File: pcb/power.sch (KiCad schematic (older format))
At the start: 6 parts

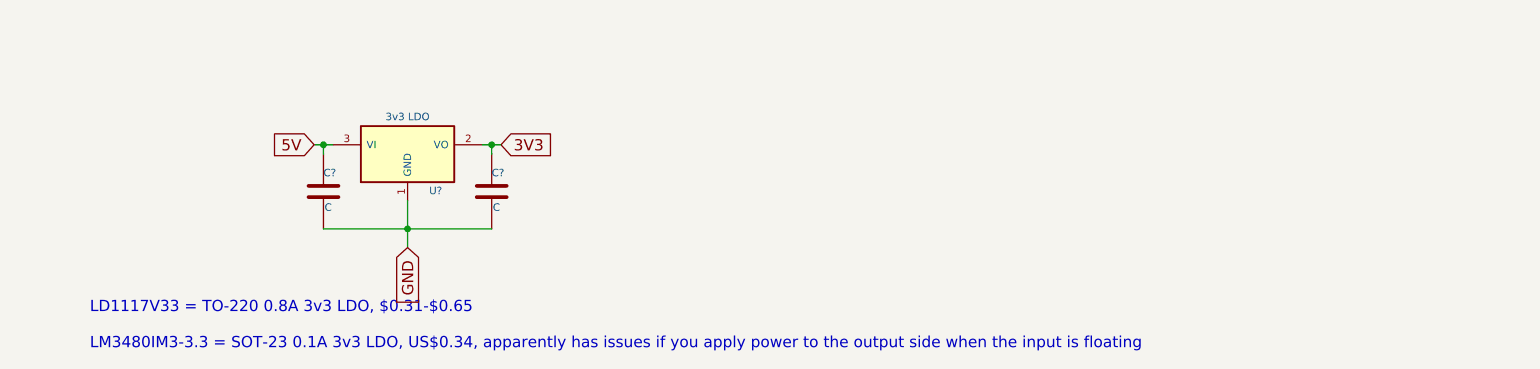
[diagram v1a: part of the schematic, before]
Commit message: added reset pullup, some caps, usb resistors, explanation for nUSB_CONNECT
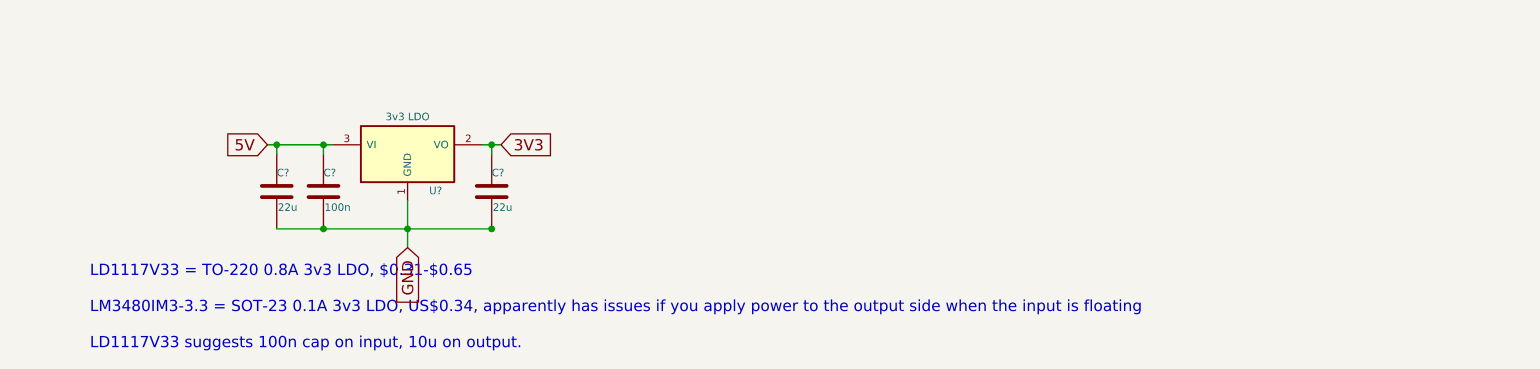
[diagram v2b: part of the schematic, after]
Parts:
- added C?: 22u, ~, symbol C
- C?: value C -> 100n
- C?: value C -> 22u
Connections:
- net 5V: now also C?.1
- net GND: now also C?.2
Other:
- note added: "LD1117V33 = TO-220 0.8A 3v3 LDO, $0.31-$0.65\n\nLM3480IM3-3.3 = SOT-23 0.1A 3v3 LDO, US$0.34, apparently has issues if you apply power to the output side when the input is floating\n\nLD1117V33 suggests 100n cap on input, 10u on output."
- note removed: "LD1117V33 = TO-220 0.8A 3v3 LDO, $0.31-$0.65\n\nLM3480IM3-3.3 = SOT-23 0.1A 3v3 LDO, US$0.34, apparently has issues if you apply power to the output side when the input is floating"
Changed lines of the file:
@@
 P 3300 4750
 F 0 "C?" H 3300 4850 40  0000 L CNN
-F 1 "C" H 3306 4665 40  0000 L CNN
+F 1 "100n" H 3306 4665 40  0000 L CNN
 F 2 "~" H 3338 4600 30  0000 C CNN
 F 3 "~" H 3300 4750 60  0000 C CNN
@@
 P 4200 4750
 F 0 "C?" H 4200 4850 40  0000 L CNN
-F 1 "C" H 4206 4665 40  0000 L CNN
+F 1 "22u" H 4206 4665 40  0000 L CNN
 F 2 "~" H 4238 4600 30  0000 C CNN
 F 3 "~" H 4200 4750 60  0000 C CNN
@@
 Wire Wire Line
 	3750 4800 3750 5050
-Wire Wire Line
-	3300 4950 4200 4950
 Connection ~ 3750 4950
-Wire Wire Line
-	4150 4500 4250 4500
 Wire Wire Line
 	4200 4500 4200 4550
 Wire Wire Line
-	3250 4500 3350 4500
-Wire Wire Line
 	3300 4500 3300 4550
-Text GLabel 3250 4500 0    60   Input ~ 0
+Text GLabel 3000 4500 0    60   Input ~ 0
 5V
 Text GLabel 4250 4500 2    60   Input ~ 0
@@
 Connection ~ 3300 4500
 Text Notes 2050 5600 0    60   ~ 0
-LD1117V33 = TO-220 0.8A 3v3 LDO, $0.31-$0.65\n\nLM3480IM3-3.3 = SOT-23 0.1A 3v3 LDO, US$0.34, apparently has issues if you apply power to the output side when the input is floating
+LD1117V33 = TO-220 0.8A 3v3 LDO, $0.31-$0.65\n\nLM3480IM3-3.3 = SOT-23 0.1A 3v3 LDO, US$0.34, apparently has issues if you apply power to the output side when the input is floating\n\nLD1117V33 suggests 100n cap on input, 10u on output.
 Text Notes 2050 3650 0    60   ~ 0
 Lipo battery connectors have power on pin 2
+$Comp
+L C C?
+U 1 1 549D6202
+P 3050 4750
+F 0 "C?" H 3050 4850 40  0000 L CNN
+F 1 "22u" H 3056 4665 40  0000 L CNN
+F 2 "~" H 3088 4600 30  0000 C CNN
+F 3 "~" H 3050 4750 60  0000 C CNN
+	1    3050 4750
+	1    0    0    -1
+$EndComp
+Wire Wire Line
+	3350 4500 3000 4500
+Wire Wire Line
+	3050 4500 3050 4550
+Connection ~ 3050 4500
+Connection ~ 3300 4950
+Connection ~ 4200 4950
+Wire Wire Line
+	4200 4950 3050 4950
+Wire Wire Line
+	4250 4500 4150 4500
 $EndSCHEMATC

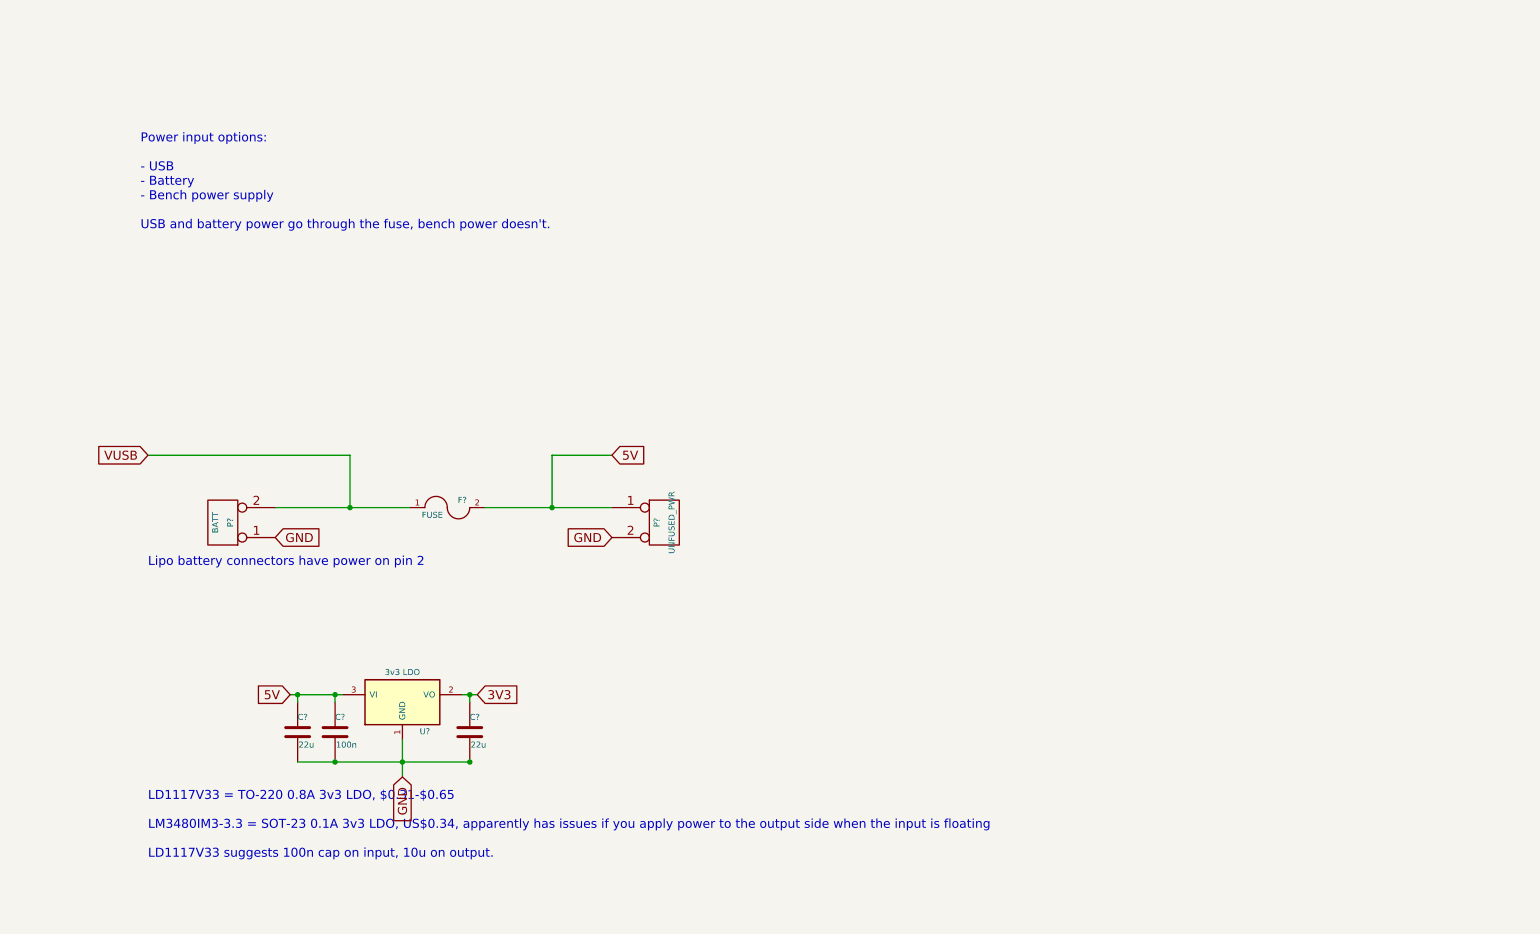
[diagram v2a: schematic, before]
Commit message: tied up some loose ends in power.sch
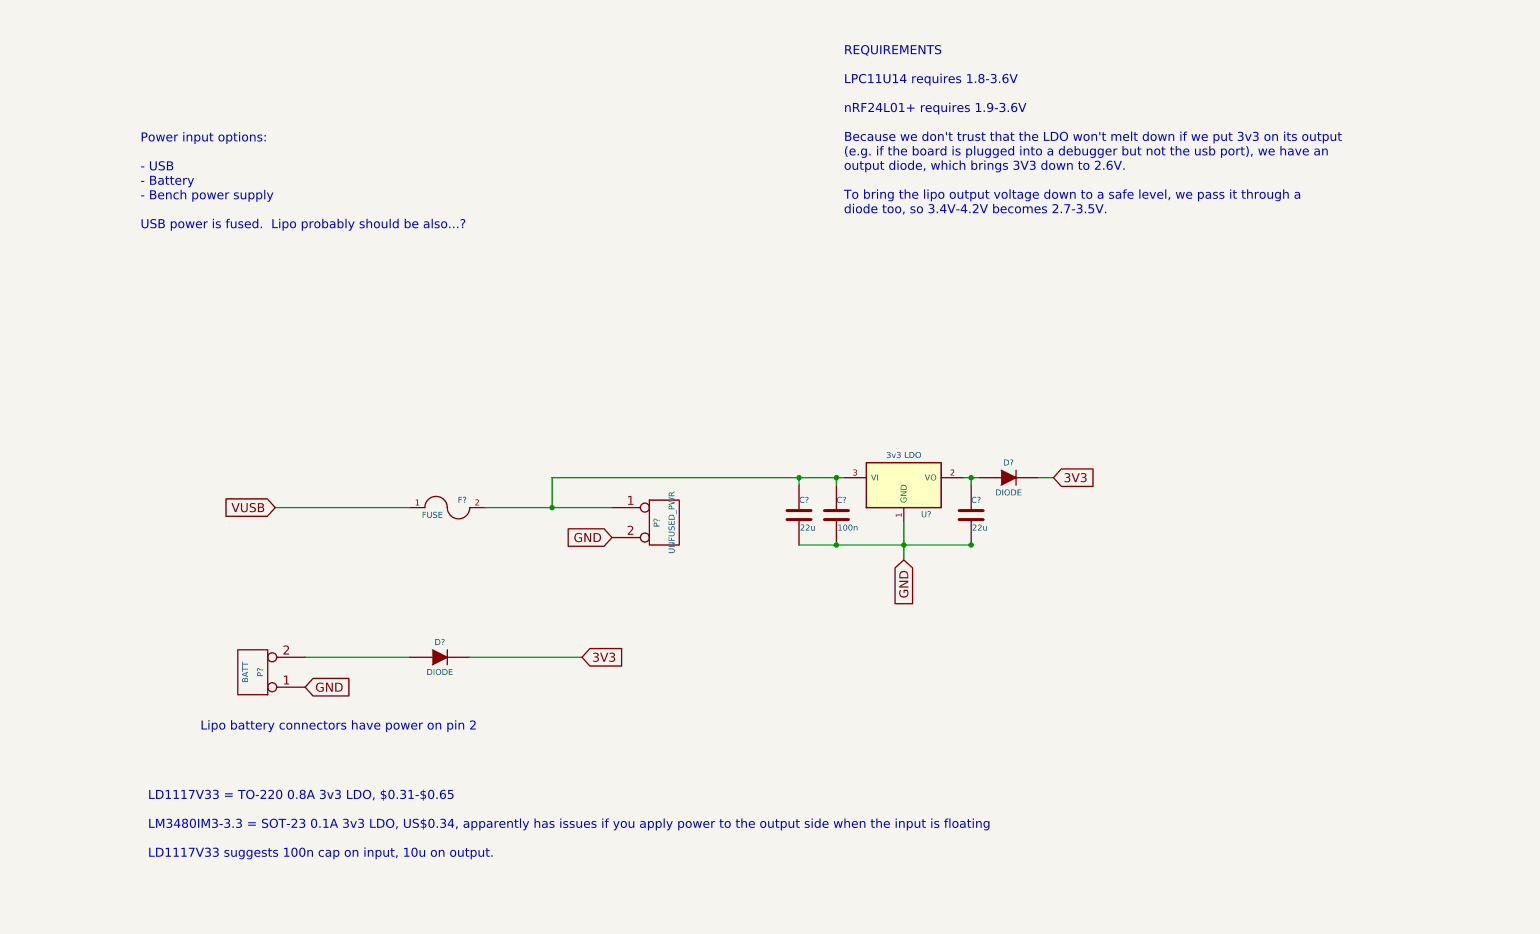
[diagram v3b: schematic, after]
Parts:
- added D? (x2): DIODE, ~, symbol DIODE
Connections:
- net 3V3: now also D?.2 (K), D?.2 (K); no longer C?.1, U?.2 (VO)
- net VUSB: no longer P?.2 (PM)
- net 5V: no longer names the net of C?.1, C?.1, F?.2, P?.1 (P1), U?.3 (VI)
- new net: D?.1 (A), P?.2 (PM)
- new net: C?.1, D?.1 (A), U?.2 (VO)
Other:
- note added: "Power input options:\n\n- USB\n- Battery\n- Bench power supply\n\nUSB power is fused. Lipo probably should be also...?"
- note added: "REQUIREMENTS\n\nLPC11U14 requires 1.8-3.6V\n\nnRF24L01+ requires 1.9-3.6V\n\nBecause we don't trust that the LDO won't melt down if we put 3v3 on its output\n(e.g. if the board is plugged into a debugger but not the usb port), we have an\noutput diode, which brings 3V3 down to 2.6V.\n\nTo bring the lipo output voltage down to a safe level, we pass it through a\ndiode too, so 3.4V-4.2V becomes 2.7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"
- note removed: "Power input options:\n\n- USB\n- Battery\n- Bench power supply\n\nUSB and battery power go through the fuse, bench power doesn't."
- moved on the sheet: C?, P?, U?
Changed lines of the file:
@@
 L CONN_2 P?
 U 1 1 549D502B
-P 2550 3350
-F 0 "P?" V 2500 3350 40  0000 C CNN
-F 1 "BATT" V 2600 3350 40  0000 C CNN
-F 2 "" H 2550 3350 60  0000 C CNN
-F 3 "" H 2550 3350 60  0000 C CNN
-	1    2550 3350
+P 2750 4350
+F 0 "P?" V 2700 4350 40  0000 C CNN
+F 1 "BATT" V 2800 4350 40  0000 C CNN
+F 2 "" H 2750 4350 60  0000 C CNN
+F 3 "" H 2750 4350 60  0000 C CNN
+	1    2750 4350
 	-1   0    0    1
 $EndComp
@@
 	1    0    0    -1
 $EndComp
-Text GLabel 2050 2900 0    60   Input ~ 0
+Text GLabel 2900 3250 0    60   Input ~ 0
 VUSB
 $Comp
@@
 Wire Wire Line
 	4300 3250 5150 3250
-Text GLabel 2900 3450 2    60   Input ~ 0
+Text GLabel 3100 4450 2    60   Input ~ 0
 GND
 Text GLabel 5150 3450 0    60   Input ~ 0
 GND
-Wire Wire Line
-	2050 2900 3400 2900
-Wire Wire Line
-	3400 2900 3400 3250
-Connection ~ 3400 3250
 Text Notes 2000 1400 0    60   ~ 0
-Power input options:\n\n- USB\n- Battery\n- Bench power supply\n\nUSB and battery power go through the fuse, bench power doesn't.
-Text GLabel 5150 2900 2    60   Input ~ 0
-5V
+Power input options:\n\n- USB\n- Battery\n- Bench power supply\n\nUSB power is fused.  Lipo probably should be also...?
 Connection ~ 4750 3250
-Wire Wire Line
-	5150 2900 4750 2900
-Wire Wire Line
-	4750 2900 4750 3250
 $Comp
 L NCP1117ST33T3G U?
 U 1 1 549D510B
-P 3750 4550
-F 0 "U?" H 3900 4354 40  0000 C CNN
-F 1 "3v3 LDO" H 3750 4750 40  0000 C CNN
-F 2 "~" H 3750 4550 60  0000 C CNN
-F 3 "~" H 3750 4550 60  0000 C CNN
-	1    3750 4550
+P 7100 3100
+F 0 "U?" H 7250 2904 40  0000 C CNN
+F 1 "3v3 LDO" H 7100 3300 40  0000 C CNN
+F 2 "~" H 7100 3100 60  0000 C CNN
+F 3 "~" H 7100 3100 60  0000 C CNN
+	1    7100 3100
 	1    0    0    -1
 $EndComp
@@
 L C C?
 U 1 1 549D5130
-P 3300 4750
-F 0 "C?" H 3300 4850 40  0000 L CNN
-F 1 "100n" H 3306 4665 40  0000 L CNN
-F 2 "~" H 3338 4600 30  0000 C CNN
-F 3 "~" H 3300 4750 60  0000 C CNN
-	1    3300 4750
+P 6650 3300
+F 0 "C?" H 6650 3400 40  0000 L CNN
+F 1 "100n" H 6656 3215 40  0000 L CNN
+F 2 "~" H 6688 3150 30  0000 C CNN
+F 3 "~" H 6650 3300 60  0000 C CNN
+	1    6650 3300
 	1    0    0    -1
 $EndComp
@@
 L C C?
 U 1 1 549D513F
-P 4200 4750
-F 0 "C?" H 4200 4850 40  0000 L CNN
-F 1 "22u" H 4206 4665 40  0000 L CNN
-F 2 "~" H 4238 4600 30  0000 C CNN
-F 3 "~" H 4200 4750 60  0000 C CNN
-	1    4200 4750
+P 7550 3300
+F 0 "C?" H 7550 3400 40  0000 L CNN
+F 1 "22u" H 7556 3215 40  0000 L CNN
+F 2 "~" H 7588 3150 30  0000 C CNN
+F 3 "~" H 7550 3300 60  0000 C CNN
+	1    7550 3300
 	1    0    0    -1
 $EndComp
-Text GLabel 3750 5050 3    60   Input ~ 0
+Text GLabel 7100 3600 3    60   Input ~ 0
 GND
 Wire Wire Line
-	3750 4800 3750 5050
-Connection ~ 3750 4950
+	7100 3350 7100 3600
+Connection ~ 7100 3500
 Wire Wire Line
-	4200 4500 4200 4550
+	7550 3050 7550 3100
 Wire Wire Line
-	3300 4500 3300 4550
-Text GLabel 3000 4500 0    60   Input ~ 0
-5V
-Text GLabel 4250 4500 2    60   Input ~ 0
+	6650 3050 6650 3100
+Text GLabel 8100 3050 2    60   Input ~ 0
 3V3
-Connection ~ 4200 4500
-Connection ~ 3300 4500
+Connection ~ 7550 3050
+Connection ~ 6650 3050
 Text Notes 2050 5600 0    60   ~ 0
 LD1117V33 = TO-220 0.8A 3v3 LDO, $0.31-$0.65\n\nLM3480IM3-3.3 = SOT-23 0.1A 3v3 LDO, US$0.34, apparently has issues if you apply power to the output side when the input is floating\n\nLD1117V33 suggests 100n cap on input, 10u on output.
-Text Notes 2050 3650 0    60   ~ 0
+Text Notes 2400 4750 0    60   ~ 0
 Lipo battery connectors have power on pin 2
 $Comp
 L C C?
 U 1 1 549D6202
-P 3050 4750
-F 0 "C?" H 3050 4850 40  0000 L CNN
-F 1 "22u" H 3056 4665 40  0000 L CNN
-F 2 "~" H 3088 4600 30  0000 C CNN
-F 3 "~" H 3050 4750 60  0000 C CNN
-	1    3050 4750
+P 6400 3300
+F 0 "C?" H 6400 3400 40  0000 L CNN
+F 1 "22u" H 6406 3215 40  0000 L CNN
+F 2 "~" H 6438 3150 30  0000 C CNN
+F 3 "~" H 6400 3300 60  0000 C CNN
+	1    6400 3300
 	1    0    0    -1
 $EndComp
 Wire Wire Line
-	3350 4500 3000 4500
+	4750 3050 6700 3050
 Wire Wire Line
-	3050 4500 3050 4550
-Connection ~ 3050 4500
-Connection ~ 3300 4950
-Connection ~ 4200 4950
+	6400 3050 6400 3100
+Connection ~ 6400 3050
+Connection ~ 6650 3500
+Connection ~ 7550 3500
 Wire Wire Line
-	4200 4950 3050 4950
+	7550 3500 6400 3500
 Wire Wire Line
-	4250 4500 4150 4500
+	7600 3050 7500 3050
+Text Notes 6700 1300 0    60   ~ 0
+REQUIREMENTS\n\nLPC11U14 requires 1.8-3.6V\n\nnRF24L01+ requires 1.9-3.6V\n\nBecause we don't trust that the LDO won't melt down if we put 3v3 on its output\n(e.g. if the board is plugged into a debugger but not the usb port), we have an\noutput diode, which brings 3V3 down to 2.6V.\n\nTo bring the lipo output voltage down to a safe level, we pass it through a\ndiode too, so 3.4V-4.2V becomes 2.7-3.5V.
+Wire Wire Line
+	4750 3250 4750 3050
+$Comp
+L DIODE D?
+U 1 1 549D6318
+P 4000 4250
+F 0 "D?" H 4000 4350 40  0000 C CNN
+F 1 "DIODE" H 4000 4150 40  0000 C CNN
+F 2 "~" H 4000 4250 60  0000 C CNN
+F 3 "~" H 4000 4250 60  0000 C CNN
+	1    4000 4250
+	1    0    0    -1
+$EndComp
+Wire Wire Line
+	3100 4250 3800 4250
+Wire Wire Line
+	4950 4250 4200 4250
+Text GLabel 4950 4250 2    60   Input ~ 0
+3V3
+$Comp
+L DIODE D?
+U 1 1 549D6438
+P 7800 3050
+F 0 "D?" H 7800 3150 40  0000 C CNN
+F 1 "DIODE" H 7800 2950 40  0000 C CNN
+F 2 "~" H 7800 3050 60  0000 C CNN
+F 3 "~" H 7800 3050 60  0000 C CNN
+	1    7800 3050
+	1    0    0    -1
+$EndComp
+Wire Wire Line
+	8100 3050 8000 3050
 $EndSCHEMATC

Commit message: thought through power situation a bit more, added some TO DO messages
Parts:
- removed D?: DIODE, ~, symbol DIODE
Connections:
- net 3V3: now also C?.1, U?.2 (VO)
- net VLED: now reaches D?.1 (A), P?.2 (PM)
- net VLED: now also C?.1, C?.1, F?.2, P?.1 (P1), U?.3 (VI)
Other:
- note added: "LD1117V33 = TO-220 0.8A 3v3 LDO, $0.31-$0.65\n\nLM3480IM3-3.3 = SOT-23 0.1A 3v3 LDO, US$0.34,\napparently has issues if you apply power to the output\nwhen the input is floating\n\nLD1117V33 suggests 100n cap on input, 10u on output."
- note added: "REQUIREMENTS\n\nLPC11U14 requires 1.8-3.6V\n\nnRF24L01+ requires 1.9-3.6V\n\nTo bring the lipo output voltage down to a safe level, we pass it through a\ndiode, so 3.4V-4.2V becomes 2.7-3.5V.\n\nWS2812B LEDs are powered from the unregulated USB or Lipo input.\n\nPOPULATE EITHER THE BATTERY CONNECTOR AND DIODE, OR\nTHE FUSE AND REGULATOR. DOING BOTH ON ONE BOARD WILL\nRESULT IN VUSB SHORTING TO 3V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"
- note removed: "LD1117V33 = TO-220 0.8A 3v3 LDO, $0.31-$0.65\n\nLM3480IM3-3.3 = SOT-23 0.1A 3v3 LDO, US$0.34, apparently has issues if you apply power to the output side when the input is floating\n\nLD1117V33 suggests 100n cap on input, 10u on output."
- note removed: "REQUIREMENTS\n\nLPC11U14 requires 1.8-3.6V\n\nnRF24L01+ requires 1.9-3.6V\n\nBecause we don't trust that the LDO won't melt down if we put 3v3 on its output\n(e.g. if the board is plugged into a debugger but not the usb port), we have an\noutput diode, which brings 3V3 down to 2.6V.\n\nTo bring the lipo output voltage down to a safe level, we pass it through a\ndiode too, so 3.4V-4.2V becomes 2.7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"
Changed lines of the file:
@@
 Connection ~ 7550 3050
 Connection ~ 6650 3050
-Text Notes 2050 5600 0    60   ~ 0
-LD1117V33 = TO-220 0.8A 3v3 LDO, $0.31-$0.65\n\nLM3480IM3-3.3 = SOT-23 0.1A 3v3 LDO, US$0.34, apparently has issues if you apply power to the output side when the input is floating\n\nLD1117V33 suggests 100n cap on input, 10u on output.
+Text Notes 6350 4050 0    60   ~ 0
+LD1117V33 = TO-220 0.8A 3v3 LDO, $0.31-$0.65\n\nLM3480IM3-3.3 = SOT-23 0.1A 3v3 LDO, US$0.34,\napparently has issues if you apply power to the output\nwhen the input is floating\n\nLD1117V33 suggests 100n cap on input, 10u on output.
 Text Notes 2400 4750 0    60   ~ 0
 Lipo battery connectors have power on pin 2
@@
 	7550 3500 6400 3500
 Wire Wire Line
-	7600 3050 7500 3050
+	7500 3050 8100 3050
 Text Notes 6700 1300 0    60   ~ 0
-REQUIREMENTS\n\nLPC11U14 requires 1.8-3.6V\n\nnRF24L01+ requires 1.9-3.6V\n\nBecause we don't trust that the LDO won't melt down if we put 3v3 on its output\n(e.g. if the board is plugged into a debugger but not the usb port), we have an\noutput diode, which brings 3V3 down to 2.6V.\n\nTo bring the lipo output voltage down to a safe level, we pass it through a\ndiode too, so 3.4V-4.2V becomes 2.7-3.5V.
+REQUIREMENTS\n\nLPC11U14 requires 1.8-3.6V\n\nnRF24L01+ requires 1.9-3.6V\n\nTo bring the lipo output voltage down to a safe level, we pass it through a\ndiode, so 3.4V-4.2V becomes 2.7-3.5V.\n\nWS2812B LEDs are powered from the unregulated USB or Lipo input.\n\nPOPULATE EITHER THE BATTERY CONNECTOR AND DIODE, OR\nTHE FUSE AND REGULATOR.  DOING BOTH ON ONE BOARD WILL\nRESULT IN VUSB SHORTING TO 3V3 THROUGH THE BATT DIODE.
 Wire Wire Line
-	4750 3250 4750 3050
+	4750 3900 4750 3050
 $Comp
 L DIODE D?
@@
 Text GLabel 4950 4250 2    60   Input ~ 0
 3V3
-$Comp
-L DIODE D?
-U 1 1 549D6438
-P 7800 3050
-F 0 "D?" H 7800 3150 40  0000 C CNN
-F 1 "DIODE" H 7800 2950 40  0000 C CNN
-F 2 "~" H 7800 3050 60  0000 C CNN
-F 3 "~" H 7800 3050 60  0000 C CNN
-	1    7800 3050
-	1    0    0    -1
-$EndComp
+Text GLabel 3200 3900 0    60   Input ~ 0
+VLED
 Wire Wire Line
-	8100 3050 8000 3050
+	3200 3900 4750 3900
+Wire Wire Line
+	3500 3900 3500 4250
+Connection ~ 3500 4250
+Connection ~ 3500 3900
 $EndSCHEMATC
